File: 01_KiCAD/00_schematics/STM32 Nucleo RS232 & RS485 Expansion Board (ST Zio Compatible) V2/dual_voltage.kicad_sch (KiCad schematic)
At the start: 25 parts, among them IC1 REG103GA-A, U3 TPS2117DRLR

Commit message: Added components and change device
Added dual Schmidt trigger input SN74LVC2G14DBV for LED Rx and Tx control.
Changed sn74hcs245 for alternate part sn74lvc245a for larger footprint and better availability with LCSC.
Difference is sn74lvc245a has no Schmidt-trigger inputs but instead just normal inputs. Fot details see dataseet. Both devices use exact same pin number and configuration except sn74lvc245a has no thermal pad or exposed pad like the sn74hcs245 has.
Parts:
- removed TP10, TP9: 5006, 5006:KEYSTONE_5006, symbol 5006_Black:5006
- renumbered C21 to C1, C16 to C10, C17 to C11, C19 to C2, C20 to C3, C13 to C4, C18 to C5, C12 to C6, C11 to C7, C14 to C8, C15 to C9, R14 to R1, R13 to R2, TP4 to TP1, TP8 to TP2, TP7 to TP3, TP5 to TP4, TP2 to TP5, TP1 to TP7, TP3 to TP8, U3 to U1
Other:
- note added: "NOTE: Place capacitors as close as possible to I/O pin."

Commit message: Finisching touches to schematics
Finalizing the schematics and double-check all connections throughout the different sheets.
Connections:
- net 3V3_SYS: now also C1.1
- net GND: now also C1.2
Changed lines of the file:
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@@
 	(symbol
 		(lib_id "Device:C_Polarized")
-		(at 232.371 63.3459 0)
+		(at 232.41 63.5 0)
 		(unit 1)
 		(exclude_from_sim no)
@@
 		(fields_autoplaced yes)
 		(property "Reference" "C1"
-			(at 236.22 59.9168 0)
+			(at 236.259 60.0709 0)
 			(effects
 				(font
@@
 		)
 		(property "Value" "100µF"
-			(at 236.22 62.4568 0)
+			(at 236.259 62.6109 0)
 			(effects
 				(font
@@
 		)
 		(property "Footprint" ""
-			(at 233.3362 67.1559 0)
+			(at 233.3752 67.31 0)
 			(effects
 				(font
@@
 		)
 		(property "Datasheet" "https://www.lcsc.com/datasheet/C401850.pdf"
-			(at 232.371 63.3459 0)
+			(at 232.41 63.5 0)
 			(effects
 				(font
@@
 		)
 		(property "Description" "100uF ±20% 50V Aluminum Electrolytic Capacitors 5000hrs@105℃"
-			(at 232.371 63.3459 0)
+			(at 232.41 63.5 0)
 			(effects
 				(font
@@
 		)
 		(property "Manufacturer" "PANASONIC"
-			(at 232.371 63.3459 0)
+			(at 232.41 63.5 0)
 			(effects
 				(font
@@
 		)
 		(property "MPN" "EEEHD1H101P"
-			(at 232.371 63.3459 0)
+			(at 232.41 63.5 0)
 			(effects
 				(font
@@
 		)
 		(property "Supplier" ""
-			(at 232.371 63.3459 0)
+			(at 232.41 63.5 0)
 			(effects
 				(font
@@
 		)
 		(property "SPN" ""
-			(at 232.371 63.3459 0)
+			(at 232.41 63.5 0)
 			(effects
 				(font
@@
 		)
 		(property "LCSC" "C401850"
-			(at 232.371 63.3459 0)
+			(at 232.41 63.5 0)
 			(effects
 				(font
@@
 		)
 		(property "Package" "SMD,D10xL10.2mm"
-			(at 232.371 63.3459 0)
+			(at 232.41 63.5 0)
 			(effects
 				(font
@@
 		)
 		(property "Type" "SMD"
-			(at 232.371 63.3459 0)
+			(at 232.41 63.5 0)
 			(effects
 				(font
@@
 		)
 		(property "DNP" ""
-			(at 232.371 63.3459 0)
+			(at 232.41 63.5 0)
 			(effects
 				(font
@@
 		)
 		(property "Dielectric" ""
-			(at 232.371 63.3459 0)
+			(at 232.41 63.5 0)
 			(effects
 				(font
@@
 		)
 		(property "Voltage Rating" "50V"
-			(at 236.22 64.9968 0)
+			(at 236.259 65.1509 0)
 			(effects
 				(font

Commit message: Finishing up the schematic aand created the board outline
Made some finishing touches to the schematic, updated all the symbol footprints and started to create the board.
Added missing 3D models for Phoenix 4-p RS485 connector and RS232 connector, also for Inolux LED.
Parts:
- C3: renamed from C1; footprint (none) -> EEEHD1H101P:CAP_EEEHD1H101P
- TP1, TP4, TP5, TP6, TP7: footprint 5005:KEYSTONE_5005 -> 5005_Red:KEYSTONE_5005
- TP2, TP3: footprint 5006:KEYSTONE_5006 -> 5006_Black:KEYSTONE_5006
- TP8: footprint 5007:KEYSTONE_5007 -> 5007_White:KEYSTONE_5007
- renumbered C2 to C1, C3 to C2
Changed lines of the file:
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@@
 		(on_board yes)
 		(dnp no)
-		(property "Reference" "C3"
+		(property "Reference" "C2"
 			(at 209.55 61.214 0)
 			(effects
@@
 			(project "STM32 Nucleo RS232 & RS485 Expansion Board (ST Zio Compatible) V2"
 				(path "/080f83b7-8913-48e8-ab8e-79cb12295542/83cf4712-deaa-472a-9432-343a24d007ba"
-					(reference "C3")
+					(reference "C2")
 					(unit 1)
 				)
@@
 		(on_board yes)
 		(dnp no)
-		(property "Reference" "C2"
+		(property "Reference" "C1"
 			(at 194.056 61.214 0)
 			(effects
@@
 			(project "STM32 Nucleo RS232 & RS485 Expansion Board (ST Zio Compatible) V2"
 				(path "/080f83b7-8913-48e8-ab8e-79cb12295542/83cf4712-deaa-472a-9432-343a24d007ba"
-					(reference "C2")
+					(reference "C1")
 					(unit 1)
 				)
@@
 		(dnp no)
 		(fields_autoplaced yes)
-		(property "Reference" "C1"
+		(property "Reference" "C3"
 			(at 236.259 60.0709 0)
 			(effects
@@
 			)
 		)
-		(property "Footprint" ""
+		(property "Footprint" "EEEHD1H101P:CAP_EEEHD1H101P"
 			(at 233.3752 67.31 0)
 			(effects
@@
 			)
 		)
-		(property "Datasheet" "https://www.lcsc.com/datasheet/C401850.pdf"
+		(property "Datasheet" "~"
 			(at 232.41 63.5 0)
 			(effects
@@
 			)
 		)
-		(property "Description" "100uF ±20% 50V Aluminum Electrolytic Capacitors 5000hrs@105℃"
+		(property "Description" "Polarized capacitor"
 			(at 232.41 63.5 0)
 			(effects
@@
 			(project ""
 				(path "/080f83b7-8913-48e8-ab8e-79cb12295542/83cf4712-deaa-472a-9432-343a24d007ba"
-					(reference "C1")
+					(reference "C3")
 					(unit 1)
 				)
@@
 			)
 		)
-		(property "Footprint" "5006:KEYSTONE_5006"
+		(property "Footprint" "5006_Black:KEYSTONE_5006"
 			(at 180.34 38.1 0)
 			(effects
@@
 	)
 	(symbol
+		(lib_name "5005_4")
 		(lib_id "5005_Red:5005")
 		(at 119.38 43.18 90)
@@
 			)
 		)
-		(property "Footprint" "5005:KEYSTONE_5005"
+		(property "Footprint" "5005_Red:KEYSTONE_5005"
 			(at 119.38 43.18 0)
 			(effects
@@
 	)
 	(symbol
+		(lib_name "5006_1")
 		(lib_id "5006_Black:5006")
 		(at 66.04 38.1 0)
@@
 			)
 		)
-		(property "Footprint" "5006:KEYSTONE_5006"
+		(property "Footprint" "5006_Black:KEYSTONE_5006"
 			(at 66.04 38.1 0)
 			(effects
@@
 			)
 		)
+		(property "Manufacturer" ""
+			(at 66.04 38.1 0)
+			(effects
+				(font
+					(size 1.27 1.27)
+				)
+				(hide yes)
+			)
+		)
+		(property "MPN" ""
+			(at 66.04 38.1 0)
+			(effects
+				(font
+					(size 1.27 1.27)
+				)
+				(hide yes)
+			)
+		)
+		(property "Supplier" ""
+			(at 66.04 38.1 0)
+			(effects
+				(font
+					(size 1.27 1.27)
+				)
+				(hide yes)
+			)
+		)
+		(property "SPN" ""
+			(at 66.04 38.1 0)
+			(effects
+				(font
+					(size 1.27 1.27)
+				)
+				(hide yes)
+			)
+		)
+		(property "LCSC" ""
+			(at 66.04 38.1 0)
+			(effects
+				(font
+					(size 1.27 1.27)
+				)
+				(hide yes)
+			)
+		)
+		(property "Type" ""
+			(at 66.04 38.1 0)
+			(effects
+				(font
+					(size 1.27 1.27)
+				)
+				(hide yes)
+			)
+		)
+		(property "DNP" ""
+			(at 66.04 38.1 0)
+			(effects
+				(font
+					(size 1.27 1.27)
+				)
+				(hide yes)
+			)
+		)
+		(property "Dielectric" ""
+			(at 66.04 38.1 0)
+			(effects
+				(font
+					(size 1.27 1.27)
+				)
+			)
+		)
+		(property "Voltage Rating" ""
+			(at 66.04 38.1 0)
+			(effects
+				(font
+					(size 1.27 1.27)
+				)
+			)
+		)
 		(pin "TP"
 		)
@@
 			)
 		)
-		(property "Footprint" "5005:KEYSTONE_5005"
+		(property "Footprint" "5005_Red:KEYSTONE_5005"
 			(at 180.34 45.72 0)
 			(effects
@@
 	)
 	(symbol
+		(lib_name "5005_2")
 		(lib_id "5005_Red:5005")
 		(at 52.07 57.15 90)
@@
 			)
 		)
-		(property "Footprint" "5005:KEYSTONE_5005"
+		(property "Footprint" "5005_Red:KEYSTONE_5005"
 			(at 52.07 57.15 0)
 			(effects
@@
 			)
 		)
-		(property "Footprint" "5007:KEYSTONE_5007"
+		(property "Footprint" "5007_White:KEYSTONE_5007"
 			(at 181.61 63.5 0)
 			(effects
@@
 	)
 	(symbol
+		(lib_name "5005_3")
 		(lib_id "5005_Red:5005")
 		(at 115.57 34.29 90)
@@
 			)
 		)
-		(property "Footprint" "5005:KEYSTONE_5005"
+		(property "Footprint" "5005_Red:KEYSTONE_5005"
 			(at 115.57 34.29 0)
 			(effects
@@
 	)
 	(symbol
+		(lib_name "5005_1")
 		(lib_id "5005_Red:5005")
 		(at 66.04 45.72 90)
@@
 			)
 		)
-		(property "Footprint" "5005:KEYSTONE_5005"
+		(property "Footprint" "5005_Red:KEYSTONE_5005"
 			(at 66.04 45.72 0)
 			(effects

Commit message: Capacitor change
Changed designator values for C1 t/m C7 so it is more logical on the sheet.
Changed capacittor C7 from 100µF to lower part of 47µF because of mechanical reasons. Old capacitor was too high and new capacitor of 47µ is just about 5-6mm in height
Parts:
- C7: renamed from C3; value 100µF -> 47µF; LCSC C401850 -> C92059; MPN EEEHD1H101P -> EEEFT1H470AP; Package SMD,D10xL10.2mm -> SMD,D6.3xL5.8mm
- renumbered C6 to C1, C7 to C2, C4 to C3, C5 to C4, C1 to C5, C2 to C6
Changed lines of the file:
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@@
 		(on_board yes)
 		(dnp no)
-		(property "Reference" "C4"
+		(property "Reference" "C3"
 			(at 110.236 67.564 0)
 			(effects
@@
 			(project "STM32 Nucleo RS232 & RS485 Expansion Board (ST Zio Compatible) V2"
 				(path "/080f83b7-8913-48e8-ab8e-79cb12295542/83cf4712-deaa-472a-9432-343a24d007ba"
-					(reference "C4")
+					(reference "C3")
 					(unit 1)
 				)
@@
 		(on_board yes)
 		(dnp no)
-		(property "Reference" "C2"
+		(property "Reference" "C6"
 			(at 209.55 61.214 0)
 			(effects
@@
 			(project "STM32 Nucleo RS232 & RS485 Expansion Board (ST Zio Compatible) V2"
 				(path "/080f83b7-8913-48e8-ab8e-79cb12295542/83cf4712-deaa-472a-9432-343a24d007ba"
-					(reference "C2")
+					(reference "C6")
 					(unit 1)
 				)
@@
 		(on_board yes)
 		(dnp no)
-		(property "Reference" "C5"
+		(property "Reference" "C4"
 			(at 141.478 74.422 0)
 			(effects
@@
 			(project "STM32 Nucleo RS232 & RS485 Expansion Board (ST Zio Compatible) V2"
 				(path "/080f83b7-8913-48e8-ab8e-79cb12295542/83cf4712-deaa-472a-9432-343a24d007ba"
-					(reference "C5")
+					(reference "C4")
 					(unit 1)
 				)
@@
 		(on_board yes)
 		(dnp no)
-		(property "Reference" "C7"
+		(property "Reference" "C2"
 			(at 60.706 76.454 0)
 			(effects
@@
 			(project "STM32 Nucleo RS232 & RS485 Expansion Board (ST Zio Compatible) V2"
 				(path "/080f83b7-8913-48e8-ab8e-79cb12295542/83cf4712-deaa-472a-9432-343a24d007ba"
-					(reference "C7")
+					(reference "C2")
 					(unit 1)
 				)
@@
 		(on_board yes)
 		(dnp no)
-		(property "Reference" "C1"
+		(property "Reference" "C5"
 			(at 194.056 61.214 0)
 			(effects
@@
 			(project "STM32 Nucleo RS232 & RS485 Expansion Board (ST Zio Compatible) V2"
 				(path "/080f83b7-8913-48e8-ab8e-79cb12295542/83cf4712-deaa-472a-9432-343a24d007ba"
-					(reference "C1")
+					(reference "C5")
 					(unit 1)
 				)
@@
 		(dnp no)
 		(fields_autoplaced yes)
-		(property "Reference" "C3"
+		(property "Reference" "C7"
 			(at 236.259 60.0709 0)
 			(effects
@@
 			)
 		)
-		(property "Value" "100µF"
+		(property "Value" "47µF"
 			(at 236.259 62.6109 0)
 			(effects
@@
 			)
 		)
-		(property "Description" "Polarized capacitor"
+		(property "Description" "47uF ±20% 50V Aluminum Electrolytic Capacitors 2000hrs@105℃"
 			(at 232.41 63.5 0)
 			(effects
@@
 			)
 		)
-		(property "MPN" "EEEHD1H101P"
+		(property "MPN" "EEEFT1H470AP"
 			(at 232.41 63.5 0)
 			(effects
@@
 			)
 		)
-		(property "LCSC" "C401850"
+		(property "LCSC" "C92059"
 			(at 232.41 63.5 0)
 			(effects
@@
 			)
 		)
-		(property "Package" "SMD,D10xL10.2mm"
+		(property "Package" "SMD,D6.3xL5.8mm"
 			(at 232.41 63.5 0)
 			(effects
@@
 			(project ""
 				(path "/080f83b7-8913-48e8-ab8e-79cb12295542/83cf4712-deaa-472a-9432-343a24d007ba"
-					(reference "C3")
+					(reference "C7")
 					(unit 1)
 				)
@@
 		(on_board yes)
 		(dnp no)
-		(property "Reference" "C6"
+		(property "Reference" "C1"
 			(at 46.736 76.454 0)
 			(effects
@@
 			(project "STM32 Nucleo RS232 & RS485 Expansion Board (ST Zio Compatible) V2"
 				(path "/080f83b7-8913-48e8-ab8e-79cb12295542/83cf4712-deaa-472a-9432-343a24d007ba"
-					(reference "C6")
+					(reference "C1")
 					(unit 1)
 				)

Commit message: Updated footprints and added components to PCB
Added some additional components to the board. Changed the footprint of the 3-pin Jumper so the bottom silkscreen text doesnlt overlap with the Dual Schmidt Trigger IC's SN74LVC2G14
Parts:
- C1, C10, C11, C2, C3, C4, C5, C6, C8, C9: PROD_ID (none) -> CAP-00810; Tolerance (none) -> 20%; Voltage (none) -> 25V

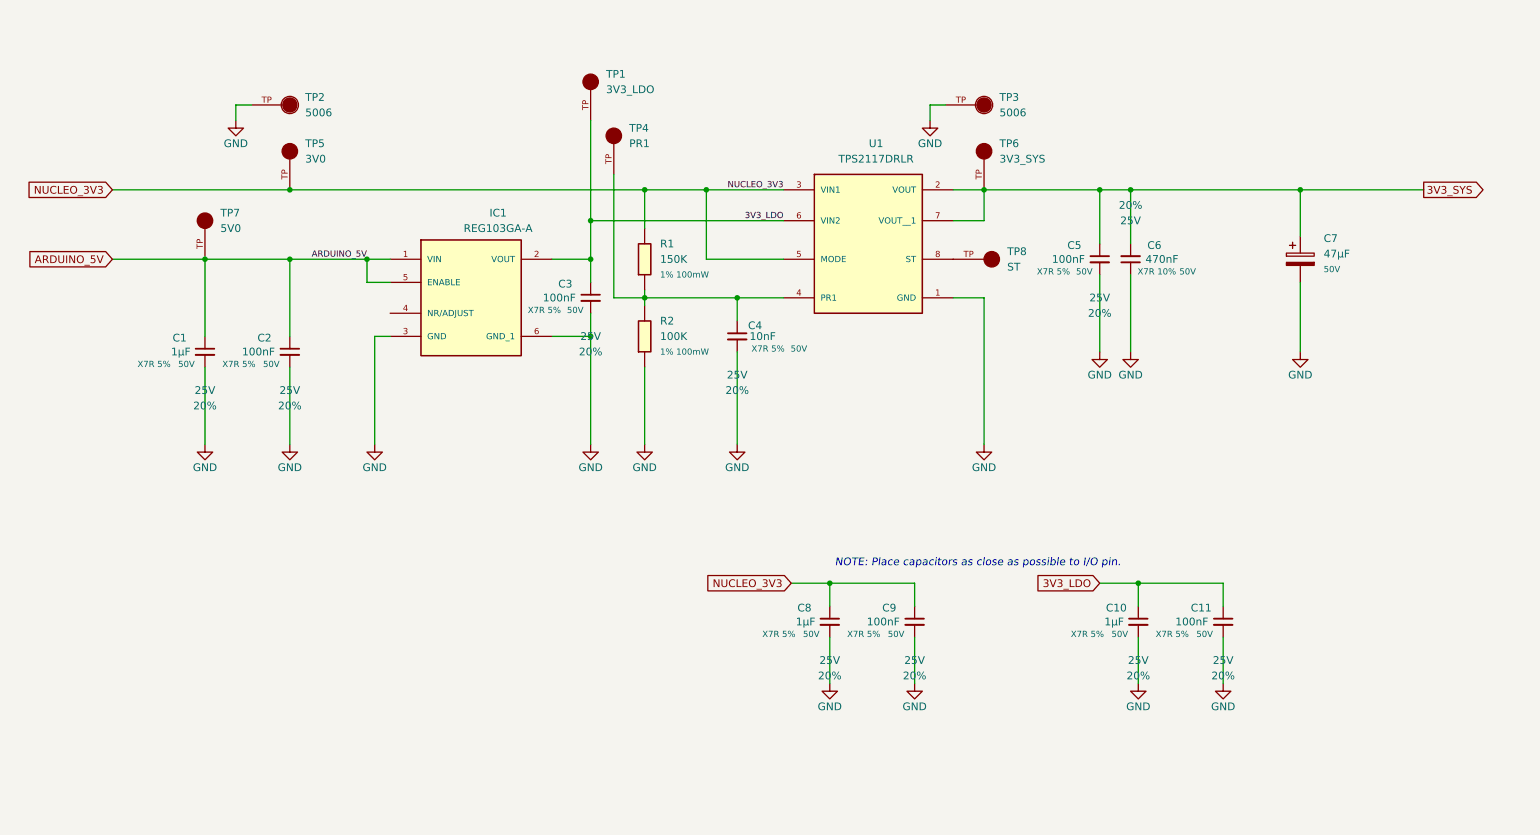
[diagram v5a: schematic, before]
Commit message: Added half-duplex jumpers
Addres jumpers for hardware RS485 half-duplex configuration combining signals A(Y) & B(Z). Finalising testpoints and added 3D models for each test-point color.
-Green = logic side
-Blue = connector side
Made some minor changed to layout for test signals clarification (THVD4431 sheet)
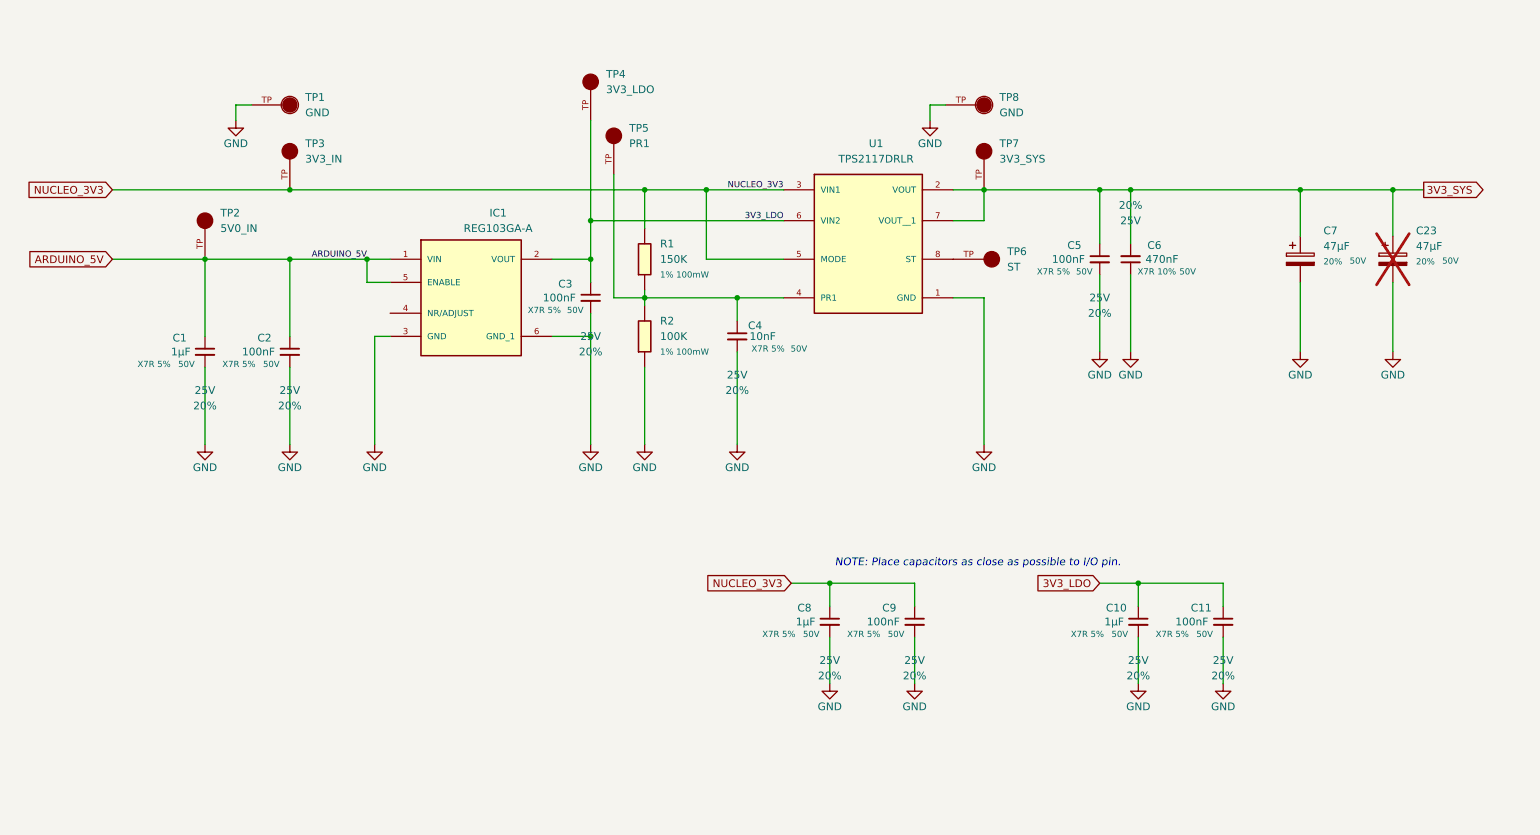
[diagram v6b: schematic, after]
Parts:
- added C23: 47µF, EEEFT1H470AP:CAP_EEEFT1H470AP, symbol Device:C_Polarized
- C7: footprint EEEHD1H101P:CAP_EEEHD1H101P -> EEEFT1H470AP:CAP_EEEFT1H470AP; Dielectric (none) -> 20%
- TP1: renamed from TP2; value 5006 -> GND
- TP2: renamed from TP7; value 5V0 -> 5V0_IN
- TP3: renamed from TP5; value 3V0 -> 3V3_IN
- TP8: renamed from TP3; value 5006 -> GND
- renumbered TP1 to TP4, TP4 to TP5, TP8 to TP6, TP6 to TP7
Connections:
- net 3V3_SYS: now also C23.1
- net GND: now also C23.2

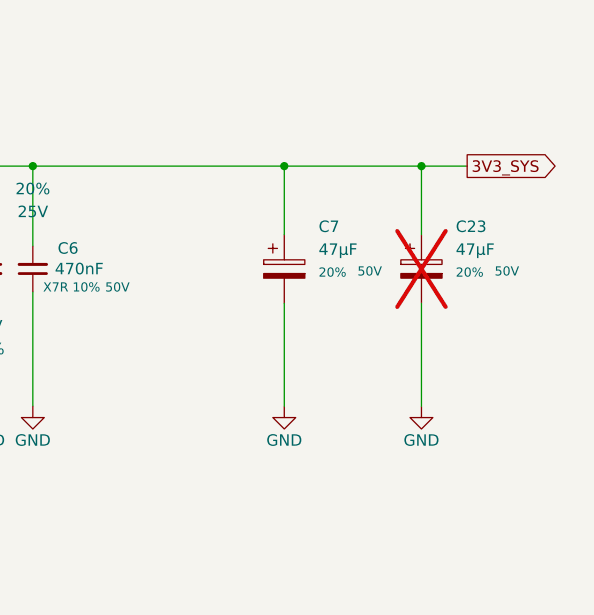
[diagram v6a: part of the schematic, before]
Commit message: Finalizing roting
Made some final routings and updated Netlist name on the schematics for some of the RS232 testpoints.
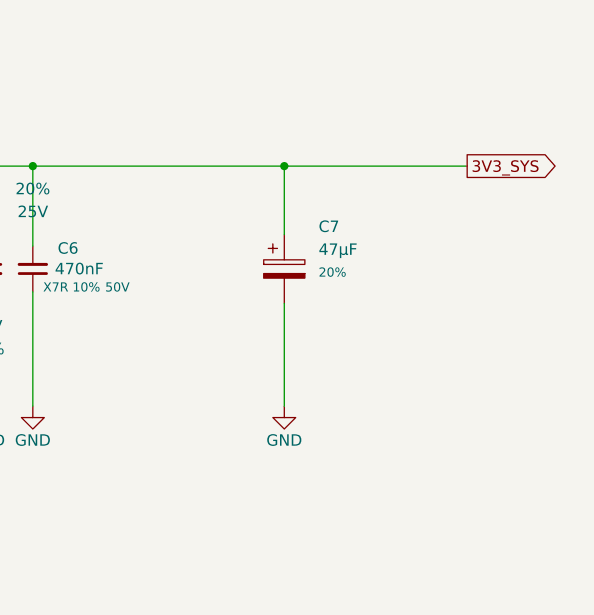
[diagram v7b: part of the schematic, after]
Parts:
- removed C23: 47µF, EEEFT1H470AP:CAP_EEEFT1H470AP, symbol Device:C_Polarized
